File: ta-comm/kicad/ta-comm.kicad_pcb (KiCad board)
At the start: 4 copper layers, 45 x 45 mm, 55 parts, among them IC1 CC1110F32RHHR, IC2 F2972NEGK, IC3 STA0693A, IC4 RFFM6404, J1 Conn_01x16, J2 Conn_01x16, J3 Conn_01x04, J4 A-1JB, J5 Conn_01x04, Y1 FOX924B-27

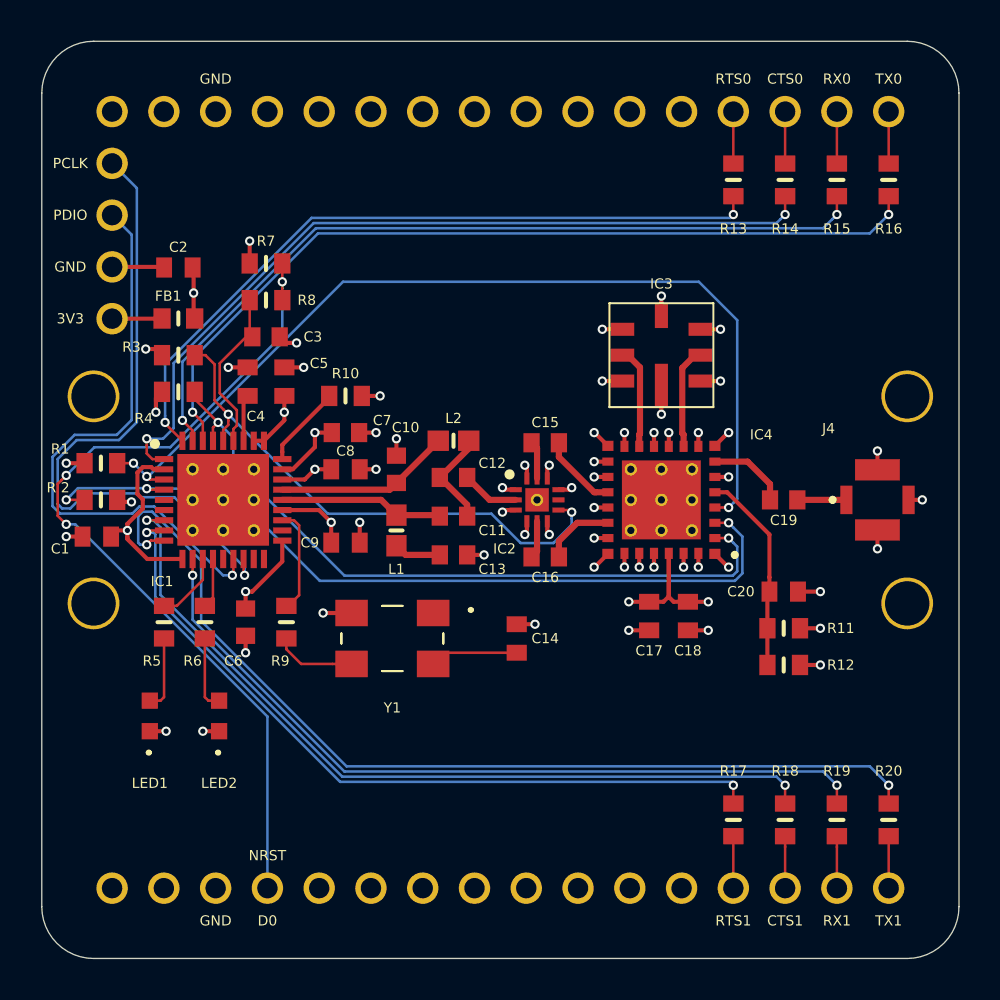
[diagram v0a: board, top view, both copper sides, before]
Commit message: Updates communication board pad and paste shapes and sizes
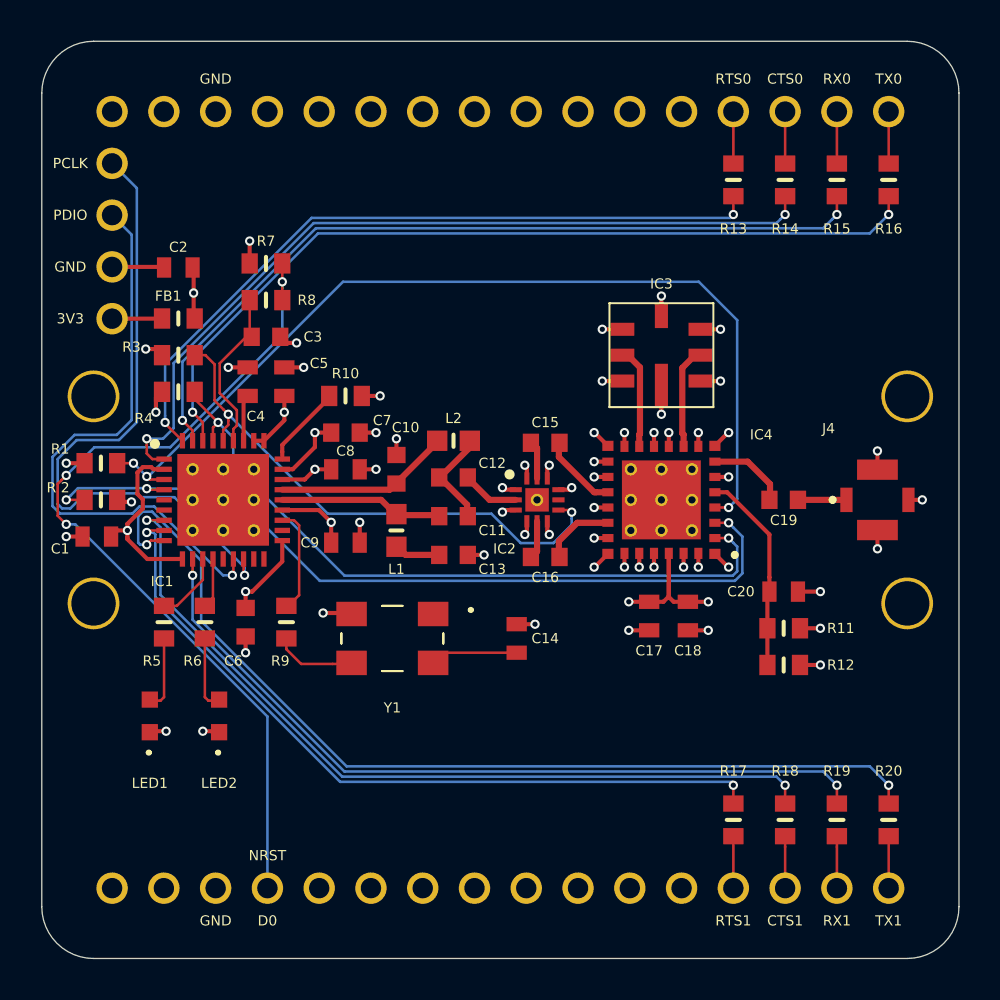
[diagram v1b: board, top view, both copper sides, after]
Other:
- rule pad_to_mask_clearance: 0.0508 -> 0.0127

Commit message: Tartan Artibeus communication board v1.0.0
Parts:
- removed R13, R14, R15, R16, R17, R18, R19, R20: MCT06030C1000FP500, ta-comm:RESC1608X55N
- added J4: Conn_01x04, ta-comm:PinSocket_1x4_TartanArtibeus, B.Cu at (135.9, 120.7)
- added J5: Conn_01x05, ta-comm:PinSocket_1x5_TartanArtibeus, F.Cu at (174.1, 95.3)
- added J6: Conn_01x05, ta-comm:PinSocket_1x5_TartanArtibeus, B.Cu at (174.1, 120.7)
- added Q1: FDY300NZ, ta-comm:SOTFL50P160X78-3N, F.Cu at (151.2, 124.0)
- moved LED2 1.40 mm to (142.6, 118.6)
- moved LED1 1.40 mm to (139.2, 118.6)
- moved C20 0.50 mm to (168.4, 112.5)
- moved R11 0.50 mm to (168.4, 114.3)
- moved R12 0.50 mm to (168.4, 116.1)
- renumbered J5 to J7, J4 to J8
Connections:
- J1 pad 13: Net-(J1-Pad13) -> /RTS0
- J1 pad 14: Net-(J1-Pad14) -> /CTS0
- J1 pad 15: Net-(J1-Pad15) -> /RX0
- J1 pad 16: Net-(J1-Pad16) -> /TX0
- J2 pad 13: Net-(J2-Pad13) -> /RTS1
- J2 pad 14: Net-(J2-Pad14) -> /CTS1
- J2 pad 15: Net-(J2-Pad15) -> /RX1
- J2 pad 16: Net-(J2-Pad16) -> /TX1
- J2 pad 3: GND -> Net-(J2-Pad3)
- J2 pad 4: /D0 -> Net-(J2-Pad4)
- J2 pad 7: Net-(J2-Pad7) -> /RST
- R7 pad 2: /D0 -> Net-(Q1-Pad3)
- R8 pad 1: /D0 -> Net-(Q1-Pad3)
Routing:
- net Net-(Q1-Pad3): track 0.00 -> 43.5 mm, vias 0 -> 4
- net /D0: track 42.8 -> 0.00 mm, vias 3 -> 0
- net /RST: track 0.00 -> 2.86 mm
- net Net-(J2-Pad16): track 2.55 -> 0.00 mm
- net Net-(J2-Pad15): track 2.55 -> 0.00 mm
- net Net-(J2-Pad14): track 2.55 -> 0.00 mm
- net Net-(J2-Pad13): track 2.55 -> 0.00 mm
- net Net-(J1-Pad16): track 2.55 -> 0.00 mm
- net Net-(J1-Pad15): track 2.55 -> 0.00 mm
- net Net-(J1-Pad14): track 2.55 -> 0.00 mm
- net Net-(J1-Pad13): track 2.55 -> 0.00 mm
- net /TX1: track 47.8 -> 49.0 mm, vias 2 -> 1
- net /TX0: track 42.2 -> 43.4 mm, vias 2 -> 1
- net /RX1: track 38.9 -> 40.0 mm, vias 2 -> 1
- net /CTS1: track 40.4 -> 41.6 mm, vias 2 -> 1
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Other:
- board text added: "J8"
- board text added: "Q1"
- board text added: "RST"
- board text added: "TA COMM v1.0.0"
- board text removed: "D0"
- board text removed: "J4"
- board text removed: "NRST"
- board text removed: "R13"
- board text removed: "R14"
- board text removed: "R15"
- board text removed: "R16"
- board text removed: "R17"
- board text removed: "R18"
- board text removed: "R19"
- board text removed: "R20"

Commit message: Tartan Artibeus communication board v1.0.1
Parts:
- removed Q1: FDY300NZ, ta-comm:SOTFL50P160X78-3N
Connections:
- C14 pad 1: Net-(C14-Pad1) -> /VDD_FILT
- J2 pad 7: /RST -> /NRST
- R7 pad 2: Net-(Q1-Pad3) -> /NRST
- R8 pad 1: Net-(Q1-Pad3) -> /NRST
- Y1 pad 4: Net-(C14-Pad1) -> /VDD_FILT
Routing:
- net /NRST: track 0.00 -> 45.7 mm, vias 0 -> 3
- net Net-(Q1-Pad3): track 43.5 -> 0.00 mm, vias 4 -> 0
- net /VDD_FILT: track 41.5 -> 46.7 mm, vias 14 -> 15
- net Net-(C14-Pad1): track 4.33 -> 0.00 mm
- net /RST: track 2.86 -> 0.00 mm
- net GND: track 49.7 -> 48.8 mm, vias 55 -> 54
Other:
- board text added: "NRST"
- board text added: "TA COMM v1.0.1"
- board text removed: "Q1"
- board text removed: "RST"
- board text removed: "TA COMM v1.0.0"
